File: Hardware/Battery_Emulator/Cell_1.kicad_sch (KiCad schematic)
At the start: 18 parts, among them Q1 IRFB7545PBF, U1 MCP4651T-103E_ST, U2 ISO1640BDR, U6 LM7805_TO220, U7 LM317_TO-220, U8 MCP6001UT-I/OT

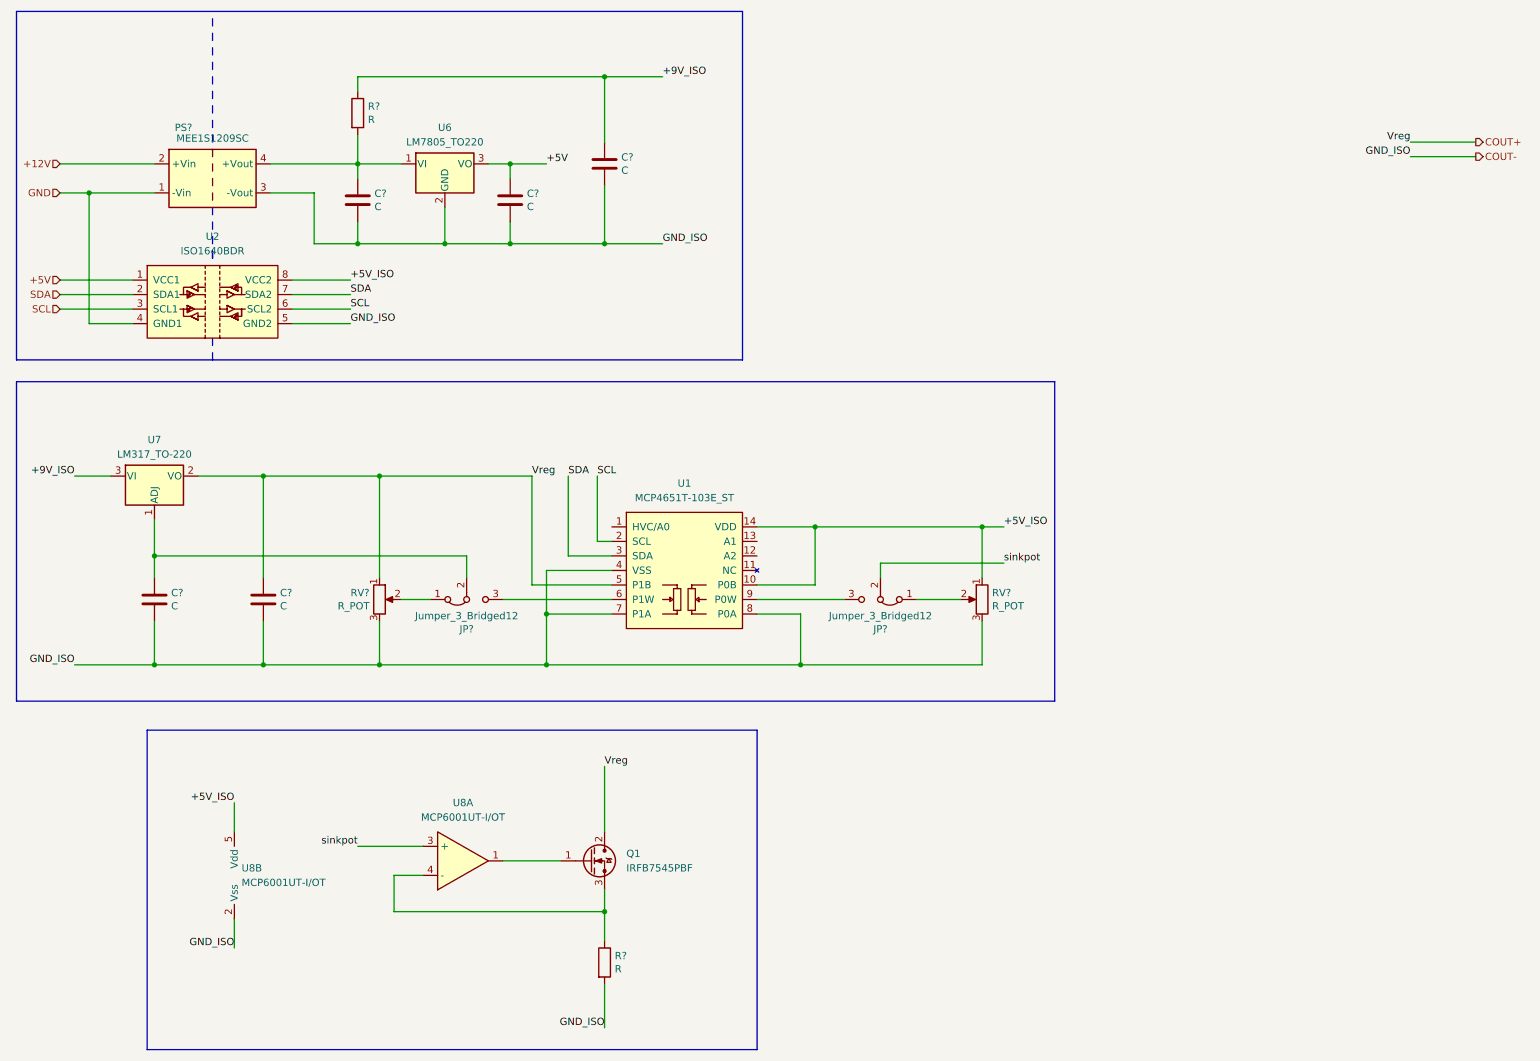
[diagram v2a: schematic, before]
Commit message: Inputted all components and values
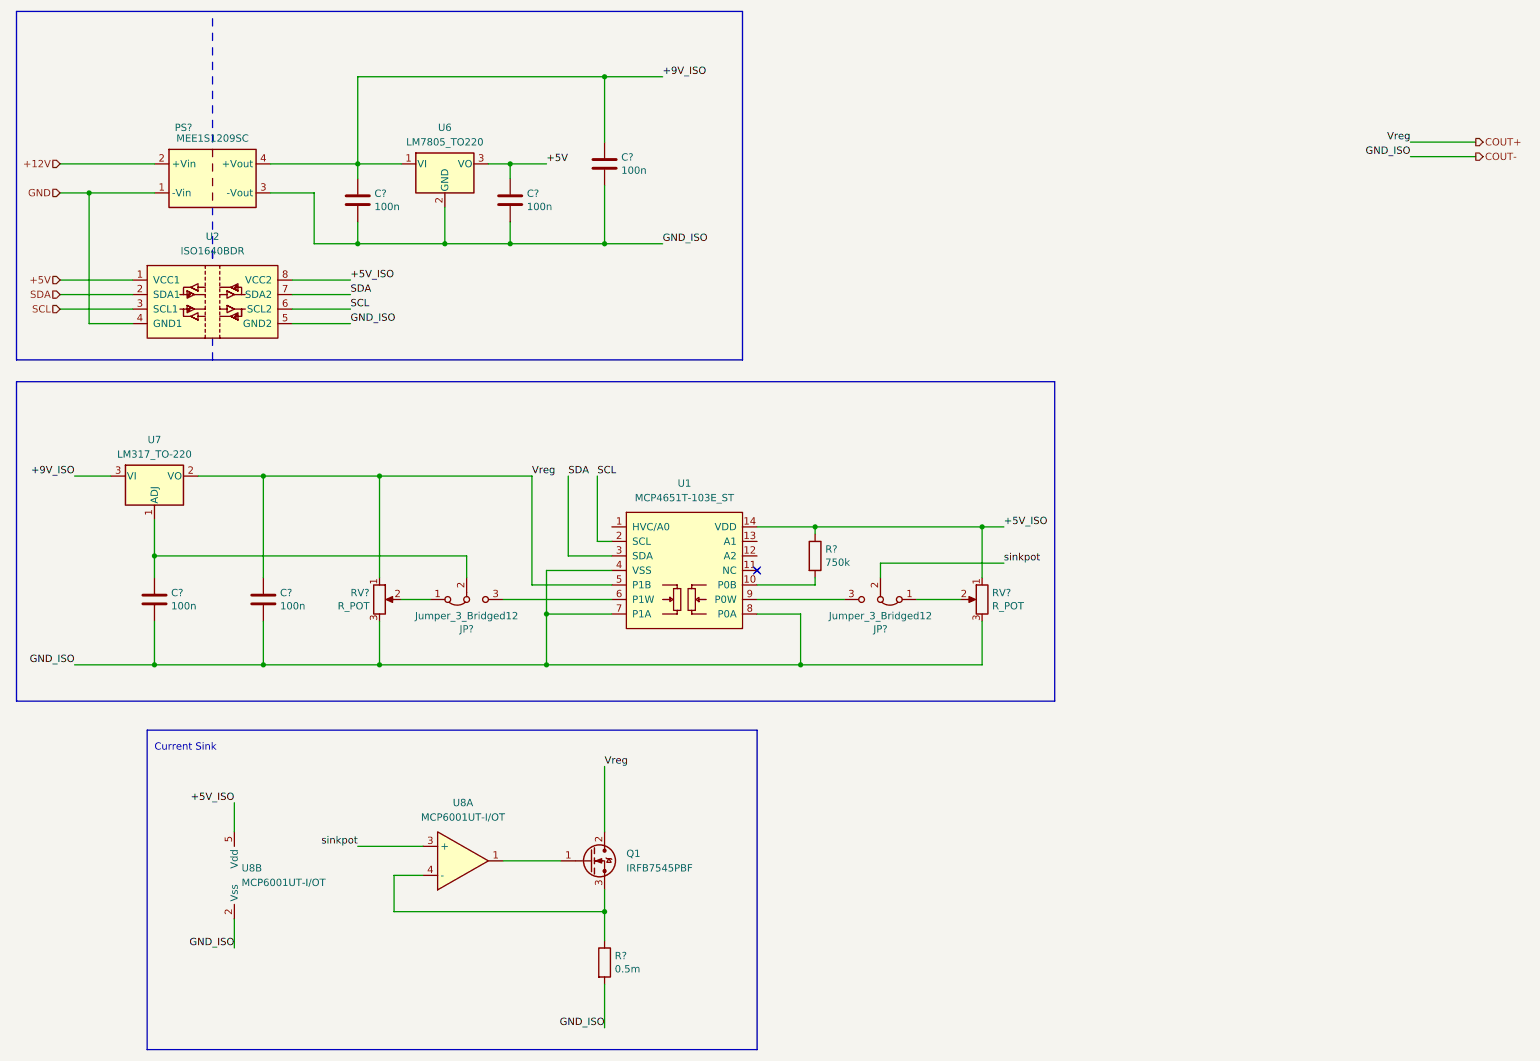
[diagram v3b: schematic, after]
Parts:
- removed R?: R, Resistor_SMD:R_0805_2012Metric, symbol Device:R
- added R?: 750k, Resistor_SMD:R_0805_2012Metric, symbol Device:R
- C? (x5): value C -> 100n
- R?: value R -> 0.5m; footprint Resistor_SMD:R_0805_2012Metric -> Resistor_SMD:R_2512_6332Metric
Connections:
- net +5V_ISO: now also R?.1; no longer U1.10 (P0B)
- net +9V_ISO: now also C?.1, PS?.4 (+Vout), U6.1 (VI)
- new net: R?.2, U1.10 (P0B)
- no-connect marks 0 -> 1
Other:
- note added: "Current Sink"
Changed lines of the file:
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@@
   (junction (at 77.47 53.34) (diameter 0) (color 0 0 0 0)
   )
+  (no_connect (at 147.32 110.49))
   (wire (pts (xy 120.65 53.34) (xy 104.14 53.34))
     (stroke (width 0) (type default))
@@
     (stroke (width 0) (type default))
   )
+  (wire (pts (xy 157.48 111.76) (xy 157.48 113.03))
+    (stroke (width 0) (type default))
+  )
   (polyline (pts (xy 52.07 52.07) (xy 52.07 53.34))
     (stroke (width 0) (type default))
@@
     (stroke (width 0) (type default))
   )
-  (wire (pts (xy 77.47 24.13) (xy 77.47 26.67))
+  (wire (pts (xy 77.47 24.13) (xy 77.47 39.37))
     (stroke (width 0) (type default))
   )
@@
     (stroke (width 0) (type default))
   )
-  (wire (pts (xy 77.47 34.29) (xy 77.47 39.37))
-    (stroke (width 0) (type default))
-  )
   (polyline (pts (xy 52.07 24.13) (xy 52.07 25.4))
     (stroke (width 0) (type default))
@@
     (stroke (width 0) (type default))
   )
-  (wire (pts (xy 157.48 102.87) (xy 157.48 113.03))
+  (wire (pts (xy 157.48 102.87) (xy 157.48 104.14))
     (stroke (width 0) (type default))
   )
@@
     (stroke (width 0) (type default))
     (fill (type none))
+  )
+  (text "Current Sink\n" (at 41.91 142.24 0)
+    (effects (font (size 1.27 1.27)) (justify left bottom))
   )
   (label "+5V" (at 110.49 39.37 0) (fields_autoplaced)
@@
       (effects (font (size 1.27 1.27)) (justify left))
     )
-    (property "Value" "C" (at 123.571 40.513 0)
+    (property "Value" "100n" (at 123.571 40.513 0)
       (effects (font (size 1.27 1.27)) (justify left))
     )
@@
         (path "/bb7641ff-0dfd-4f4a-b3be-57afbbb9fdac/86a0f187-fc20-4f8c-b621-2752c8234446"
           (reference "C6") (unit 1)
-        )
-      )
-    )
-  )
-  (symbol (lib_id "Device:R") (at 77.47 30.48 0) (unit 1)
-    (in_bom yes) (on_board yes) (dnp no)
-    (property "Reference" "R?" (at 79.248 29.3116 0)
-      (effects (font (size 1.27 1.27)) (justify left))
-    )
-    (property "Value" "R" (at 79.248 31.623 0)
-      (effects (font (size 1.27 1.27)) (justify left))
-    )
-    (property "Footprint" "Resistor_SMD:R_0805_2012Metric" (at 75.692 30.48 90)
-      (effects (font (size 1.27 1.27)) hide)
-    )
-    (property "Datasheet" "~" (at 77.47 30.48 0)
-      (effects (font (size 1.27 1.27)) hide)
-    )
-    (pin "1")
-    (pin "2")
-    (instances
-      (project "Battery_Emulator"
-        (path "/bb7641ff-0dfd-4f4a-b3be-57afbbb9fdac"
-          (reference "R?") (unit 1)
-        )
-        (path "/bb7641ff-0dfd-4f4a-b3be-57afbbb9fdac/86a0f187-fc20-4f8c-b621-2752c8234446"
-          (reference "R5") (unit 1)
         )
       )
@@
       (effects (font (size 1.27 1.27)) (justify left))
     )
-    (property "Value" "R" (at 122.428 180.213 0)
-      (effects (font (size 1.27 1.27)) (justify left))
-    )
-    (property "Footprint" "Resistor_SMD:R_0805_2012Metric" (at 118.872 179.07 90)
-      (effects (font (size 1.27 1.27)) hide)
-    )
-    (property "Datasheet" "~" (at 120.65 179.07 0)
+    (property "Value" "0.5m" (at 122.428 180.213 0)
+      (effects (font (size 1.27 1.27)) (justify left))
+    )
+    (property "Footprint" "Resistor_SMD:R_2512_6332Metric" (at 118.872 179.07 90)
+      (effects (font (size 1.27 1.27)) hide)
+    )
+    (property "Datasheet" "https://nl.mouser.com/ProductDetail/Ohmite/PCS2512FR0050ET?qs=sGAEpiMZZMtlleCFQhR%2FzRH%2FPnzm6Qg0HsYmtkKDwHfIXEJ4ch5rIQ%3D%3D" (at 120.65 179.07 0)
       (effects (font (size 1.27 1.27)) hide)
     )
@@
       (effects (font (size 1.27 1.27)) (justify left))
     )
-    (property "Value" "C" (at 44.831 116.713 0)
+    (property "Value" "100n" (at 44.831 116.713 0)
       (effects (font (size 1.27 1.27)) (justify left))
     )
@@
       (effects (font (size 1.27 1.27)) (justify left))
     )
-    (property "Value" "C" (at 63.881 116.713 0)
+    (property "Value" "100n" (at 63.881 116.713 0)
       (effects (font (size 1.27 1.27)) (justify left))
     )
@@
     )
   )
+  (symbol (lib_id "Device:R") (at 157.48 107.95 0) (unit 1)
+    (in_bom yes) (on_board yes) (dnp no)
+    (property "Reference" "R?" (at 159.258 106.7816 0)
+      (effects (font (size 1.27 1.27)) (justify left))
+    )
+    (property "Value" "750k" (at 159.258 109.093 0)
+      (effects (font (size 1.27 1.27)) (justify left))
+    )
+    (property "Footprint" "Resistor_SMD:R_0805_2012Metric" (at 155.702 107.95 90)
+      (effects (font (size 1.27 1.27)) hide)
+    )
+    (property "Datasheet" "~" (at 157.48 107.95 0)
+      (effects (font (size 1.27 1.27)) hide)
+    )
+    (pin "1")
+    (pin "2")
+    (instances
+      (project "Battery_Emulator"
+        (path "/bb7641ff-0dfd-4f4a-b3be-57afbbb9fdac"
+          (reference "R?") (unit 1)
+        )
+        (path "/bb7641ff-0dfd-4f4a-b3be-57afbbb9fdac/86a0f187-fc20-4f8c-b621-2752c8234446"
+          (reference "R1") (unit 1)
+        )
+      )
+    )
+  )
   (symbol (lib_id "PR7 Custom:IRFB7545PBF") (at 120.65 161.29 0) (unit 1)
     (in_bom yes) (on_board yes) (dnp no) (fields_autoplaced)
@@
       (effects (font (size 1.27 1.27)) (justify left))
     )
-    (property "Value" "C" (at 107.061 46.863 0)
+    (property "Value" "100n" (at 107.061 46.863 0)
       (effects (font (size 1.27 1.27)) (justify left))
     )
@@
       (effects (font (size 1.27 1.27)) (justify left))
     )
-    (property "Value" "C" (at 80.391 46.863 0)
-      (effects (font (size 1.27 1.27)) (justify left))
-    )
+    (property "Value" "100n" (at 80.391 46.863 0)
+      (effects (font (size 1.27 1.27)) (justify left))
+    )

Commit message: Updated schematic battery emulator
Made schematic more clear. Fixed some bugs
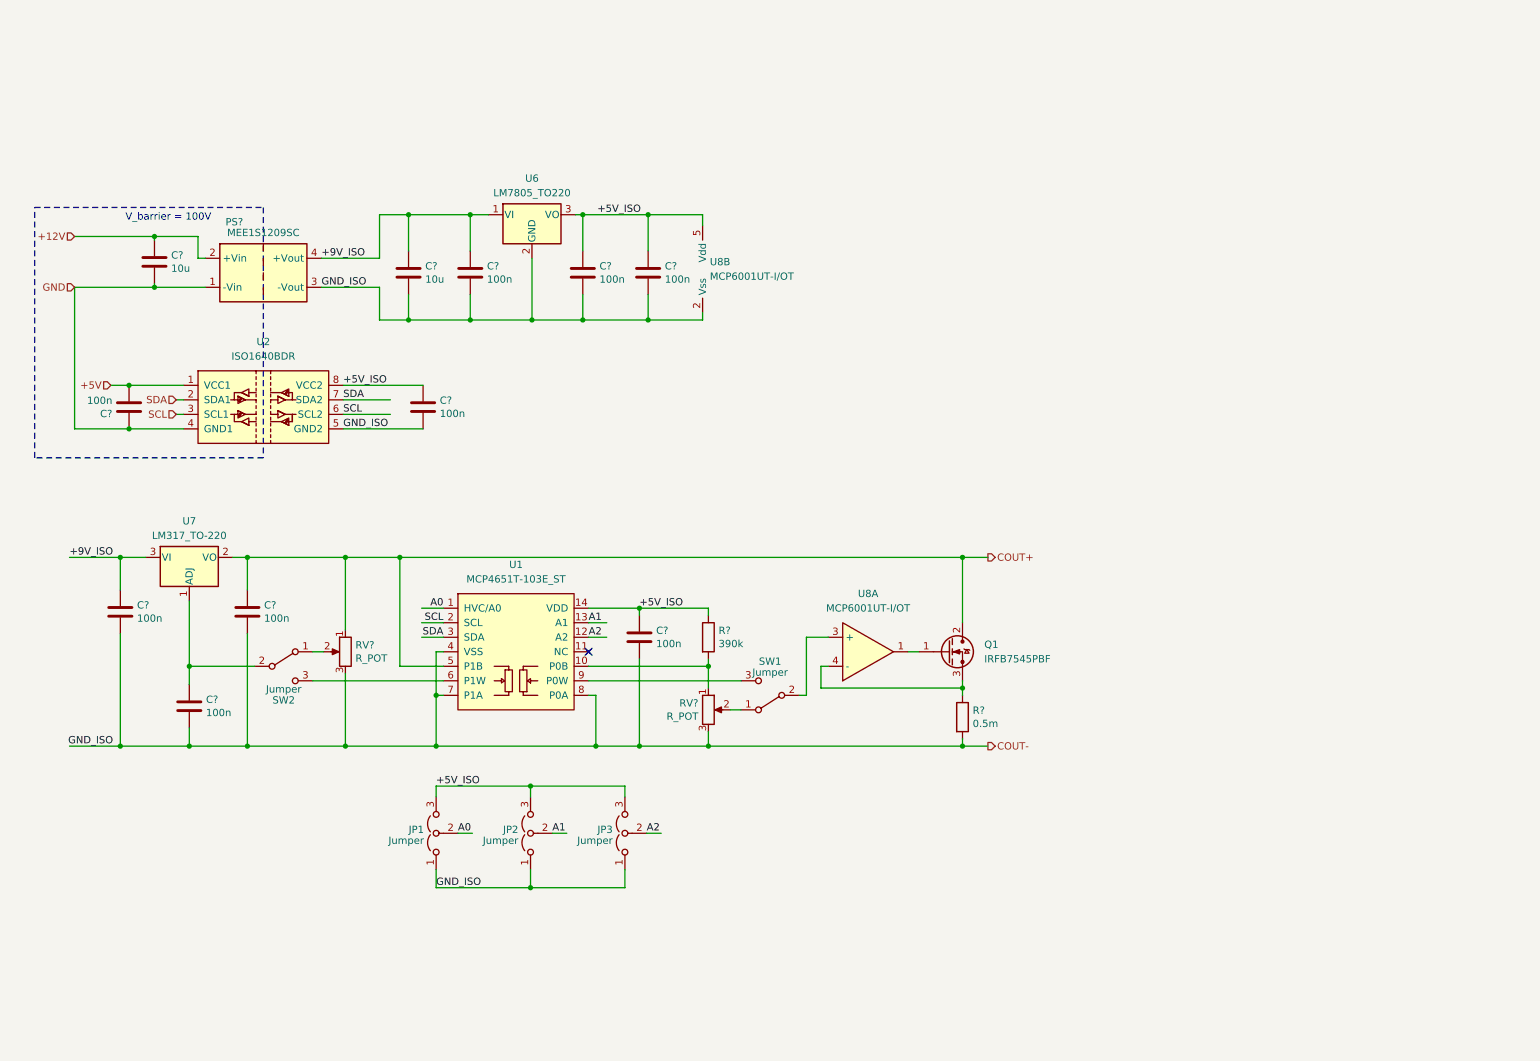
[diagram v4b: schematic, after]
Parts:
- removed JP? (x2): Jumper_3_Bridged12, symbol Jumper:Jumper_3_Bridged12
- added C? (x4): 100n, Capacitor_SMD:C_0805_2012Metric, symbol Device:C
- added C? (x2): 10u, Capacitor_SMD:C_0805_2012Metric, symbol Device:C
- added JP1, JP2, JP3: Jumper, symbol Jumper:Jumper_3_Open
- added SW1, SW2: Jumper, Jumper:SolderJumper-3_P1.3mm_Open_Pad1.0x1.5mm, symbol Switch:SW_SPDT
- R?: value 750k -> 390k
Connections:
- net +12V: now also C?.1
- net +5V: now also C?.2; no longer C?.1, U6.3 (VO)
- net +5V_ISO: now also C?.1, U6.3 (VO), C?.1, C?.1, C?.1, JP1.3 (B), JP2.3 (B), JP3.3 (B); no longer RV?.1
- net +9V_ISO: now also C?.1
- net COUT-: now also C?.2, C?.2, C?.2, C?.2, JP1.1 (A), JP2.1 (A), JP3.1 (A)
- net GND: now also C?.1, C?.2
- net at RV?.2: now also SW1.1 (A)
- net at U1.9 (P0W): now also SW1.3 (C)
- net at RV?.2: now also SW2.1 (A)
- net at C?.1, U7.1 (ADJ): now also SW2.2 (B)
- net at U1.6 (P1W): now also SW2.3 (C)
- net A0: now reaches U1.1 (HVC/A0)
- net A0: now also JP1.2 (C)
- net at R?.2, U1.10 (P0B): now also RV?.1
- net A2: now reaches U1.12 (A2)
- net A2: now also JP3.2 (C)
- net A1: now reaches U1.13 (A1)
- net A1: now also JP2.2 (C)
- net sinkpot: no longer names the net of U8.3 (+)
- net sinkpot: now also SW1.2 (B)
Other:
- note added: "V_barrier = 100V"
- note removed: "Current Sink"
- moved on the sheet: C?, PS?, Q1, R?, RV?, U1, U2, U6, U7, U8A, U8B

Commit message: Added components to PCB and started the layout
Also added footprints for the pots, jumpers and power connector
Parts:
- JP1, JP2, JP3: footprint (none) -> Jumper:SolderJumper-3_P1.3mm_Open_Pad1.0x1.5mm_NumberLabels
- RV? (x2): footprint (none) -> Potentiometer_THT:Potentiometer_Bourns_PTA3043_Single_Slide
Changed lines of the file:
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@@
       (effects (font (size 1.27 1.27)) (justify right))
     )
-    (property "Footprint" "" (at 138.811 134.874 0)
-      (effects (font (size 1.27 1.27)) hide)
-    )
-    (property "Datasheet" "~" (at 138.811 134.874 0)
+    (property "Footprint" "Potentiometer_THT:Potentiometer_Bourns_PTA3043_Single_Slide" (at 138.811 134.874 0)
+      (effects (font (size 1.27 1.27)) hide)
+    )
+    (property "Datasheet" "https://nl.mouser.com/ProductDetail/Bourns/PTA3043-2010CIB102?qs=h2IHEVivlqABjHDuBA6rbg%3D%3D" (at 138.811 134.874 0)
       (effects (font (size 1.27 1.27)) hide)
     )
@@
       (effects (font (size 1.27 1.27)) (justify left))
     )
-    (property "Footprint" "" (at 124.206 156.464 0)
+    (property "Footprint" "Jumper:SolderJumper-3_P1.3mm_Open_Pad1.0x1.5mm_NumberLabels" (at 124.206 156.464 0)
       (effects (font (size 1.27 1.27)) hide)
     )
@@
       (effects (font (size 1.27 1.27)) (justify right))
     )
-    (property "Footprint" "" (at 75.311 124.714 0)
-      (effects (font (size 1.27 1.27)) hide)
-    )
-    (property "Datasheet" "~" (at 75.311 124.714 0)
+    (property "Footprint" "Potentiometer_THT:Potentiometer_Bourns_PTA3043_Single_Slide" (at 75.311 124.714 0)
+      (effects (font (size 1.27 1.27)) hide)
+    )
+    (property "Datasheet" "https://nl.mouser.com/ProductDetail/Bourns/PTA3043-2010CIB102?qs=h2IHEVivlqABjHDuBA6rbg%3D%3D" (at 75.311 124.714 0)
       (effects (font (size 1.27 1.27)) hide)
     )
@@
       (effects (font (size 1.27 1.27)) (justify left))
     )
-    (property "Footprint" "" (at 91.186 156.464 0)
+    (property "Footprint" "Jumper:SolderJumper-3_P1.3mm_Open_Pad1.0x1.5mm_NumberLabels" (at 91.186 156.464 0)
       (effects (font (size 1.27 1.27)) hide)
     )
@@
       (effects (font (size 1.27 1.27)) (justify left))
     )
-    (property "Footprint" "" (at 107.696 156.464 0)
-      (effects (font (size 1.27 1.27)) hide)
-    )
+    (property "Footprint" "Jumper:SolderJumper-3_P1.3mm_Open_Pad1.0x1.5mm_NumberLabels" (at 107.696 156.464 0)
+      (effects (font (size 1.27 1.27)) hide)
+    )
